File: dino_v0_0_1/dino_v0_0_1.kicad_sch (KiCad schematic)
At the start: 27 parts, among them Q1 Write Button Gate, U1 Quad AND

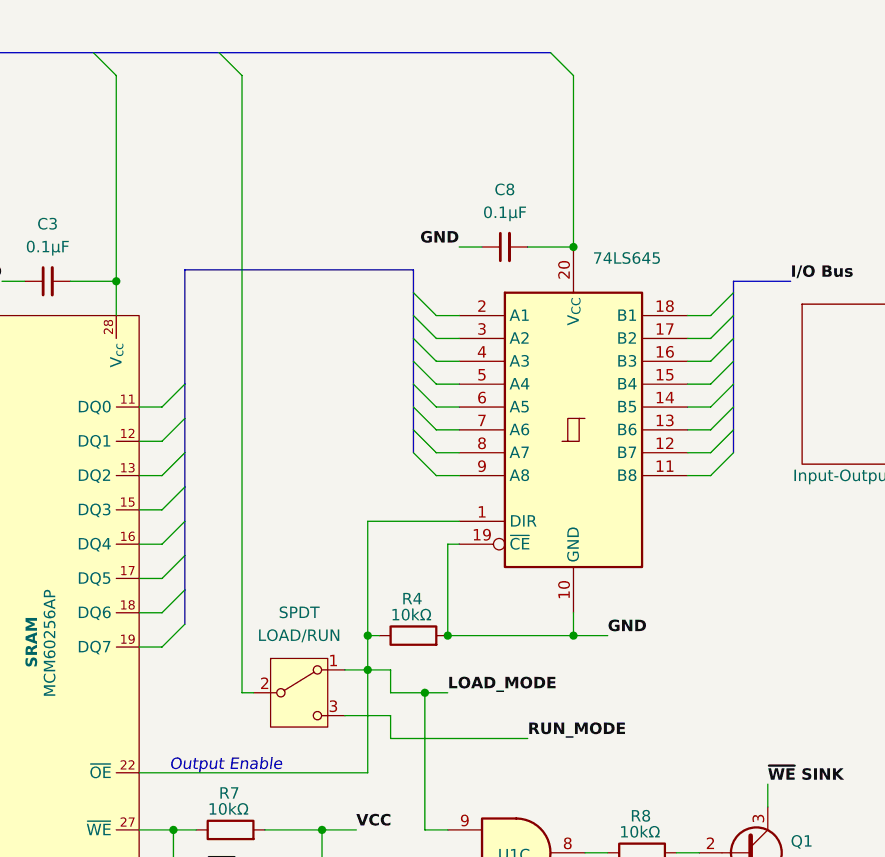
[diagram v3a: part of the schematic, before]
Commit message: Refactors circuit schematic and adds component
Repositions resistors and re-routes junctions for optimized layout.
Introduces 74LS244N component to enhance functionality.
Updates buses and wires for improved organization and signal integrity.
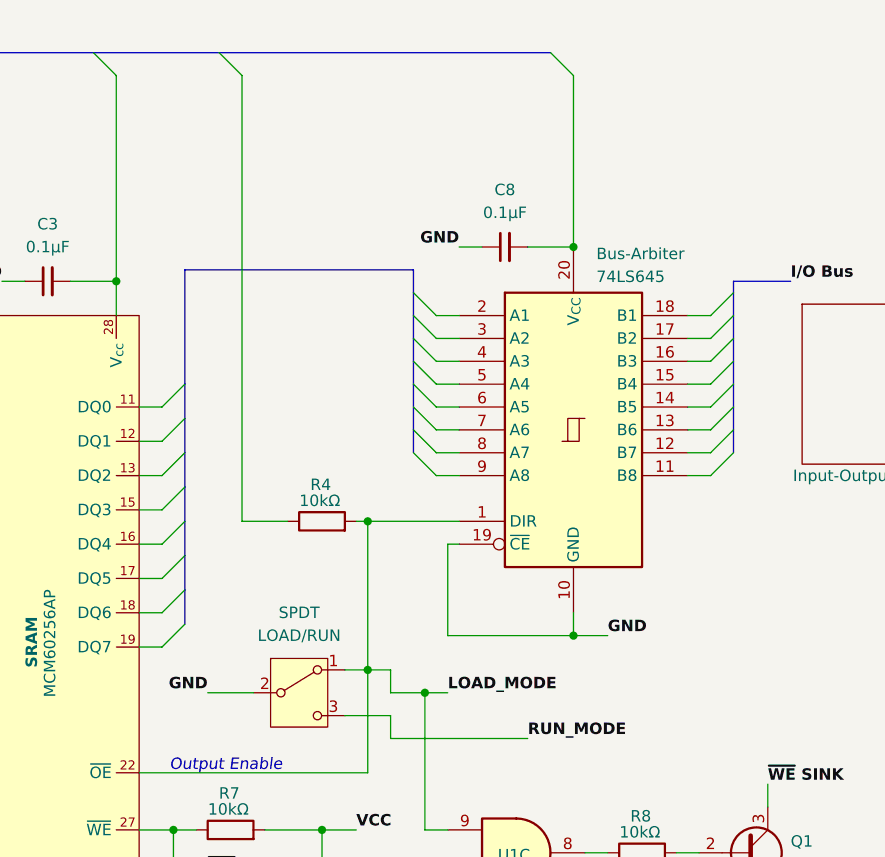
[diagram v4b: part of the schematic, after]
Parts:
- Bus-Arbiter: renamed from 74LS645; value ~ -> 74LS645
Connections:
- net GND: now also SPDT.2 (B); no longer R4.2
- net LOAD_MODE: now also R4.2; no longer R4.1
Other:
- moved on the sheet: R4
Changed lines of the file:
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@@
 	)
 	(junction
-		(at 199.39 82.55)
-		(diameter 0)
-		(color 0 0 0 0)
-	)
-	(junction
 		(at 171.45 43.18)
 		(diameter 0)
@@
 	)
 	(junction
-		(at 199.39 86.36)
+		(at 199.39 69.85)
 		(diameter 0)
 		(color 0 0 0 0)
 	)
 	(junction
-		(at 208.28 82.55)
+		(at 199.39 86.36)
 		(diameter 0)
 		(color 0 0 0 0)
@@
 	(wire
 		(pts
+			(xy 199.39 69.85) (xy 209.55 69.85)
+		)
+		(stroke
+			(width 0)
+			(type default)
+		)
+	)
+	(wire
+		(pts
 			(xy 49.53 36.83) (xy 49.53 38.1)
 		)
@@
 	(wire
 		(pts
+			(xy 199.39 69.85) (xy 199.39 86.36)
+		)
+		(stroke
+			(width 0)
+			(type default)
+		)
+	)
+	(wire
+		(pts
 			(xy 201.93 93.98) (xy 217.17 93.98)
 		)
@@
 		)
 	)
-	(wire
-		(pts
-			(xy 199.39 82.55) (xy 199.39 86.36)
-		)
-		(stroke
-			(width 0)
-			(type default)
-		)
-	)
 	(bus
 		(pts
@@
 		)
 	)
+	(wire
+		(pts
+			(xy 181.61 88.9) (xy 186.69 88.9)
+		)
+		(stroke
+			(width 0)
+			(type default)
+		)
+	)
+	(wire
+		(pts
+			(xy 198.12 69.85) (xy 199.39 69.85)
+		)
+		(stroke
+			(width 0)
+			(type default)
+		)
+	)
 	(bus
 		(pts
@@
 	(wire
 		(pts
-			(xy 185.42 20.32) (xy 185.42 88.9)
-		)
-		(stroke
-			(width 0)
-			(type default)
-		)
-	)
-	(wire
-		(pts
 			(xy 93.98 143.51) (xy 101.6 143.51)
 		)
@@
 		)
 	)
+	(wire
+		(pts
+			(xy 185.42 20.32) (xy 185.42 69.85)
+		)
+		(stroke
+			(width 0)
+			(type default)
+		)
+	)
 	(bus
 		(pts
@@
 	(wire
 		(pts
-			(xy 95.25 113.03) (xy 105.41 113.03)
+			(xy 185.42 69.85) (xy 190.5 69.85)
 		)
 		(stroke
@@
 		)
 	)
-	(bus
+	(wire
 		(pts
-			(xy 179.07 77.47) (xy 179.07 73.66)
+			(xy 95.25 113.03) (xy 105.41 113.03)
 		)
 		(stroke
@@
 		)
 	)
-	(wire
+	(bus
 		(pts
-			(xy 87.63 140.97) (xy 87.63 143.51)
+			(xy 179.07 77.47) (xy 179.07 73.66)
 		)
 		(stroke
@@
 	(wire
 		(pts
-			(xy 199.39 82.55) (xy 200.66 82.55)
+			(xy 87.63 140.97) (xy 87.63 143.51)
 		)
 		(stroke
@@
 	(wire
 		(pts
-			(xy 199.39 69.85) (xy 199.39 82.55)
-		)
-		(stroke
-			(width 0)
-			(type default)
-		)
-	)
-	(wire
-		(pts
 			(xy 234.95 59.69) (xy 237.49 59.69)
 		)
@@
 	(wire
 		(pts
-			(xy 186.69 88.9) (xy 185.42 88.9)
-		)
-		(stroke
-			(width 0)
-			(type default)
-		)
-	)
-	(wire
-		(pts
 			(xy 234.95 62.23) (xy 237.49 62.23)
 		)
@@
 		)
 	)
-	(wire
-		(pts
-			(xy 209.55 69.85) (xy 199.39 69.85)
-		)
-		(stroke
-			(width 0)
-			(type default)
-		)
-	)
 	(bus
 		(pts
@@
 		)
 	)
+	(label "GND"
+		(at 181.61 88.9 180)
+		(effects
+			(font
+				(size 1.27 1.27)
+				(thickness 0.254)
+				(bold yes)
+				(color 0 0 0 1)
+			)
+			(justify right bottom)
+		)
+	)
 	(label "RUN_MODE"
 		(at 60.96 59.69 180)
@@
 		(on_board yes)
 		(dnp no)
-		(fields_autoplaced yes)
-		(property "Reference" "74LS645"
-			(at 224.3933 40.64 0)
+		(property "Reference" "Bus-Arbiter"
+			(at 224.79 40.132 0)
 			(effects
 				(font
@@
 			)
 		)
-		(property "Value" "~"
-			(at 224.3933 43.18 0)
+		(property "Value" "74LS645"
+			(at 224.79 42.672 0)
 			(effects
 				(font
@@
 			(project ""
 				(path "/e43166a5-d972-471d-b3cf-9f4f12c7f541"
-					(reference "74LS645")
+					(reference "Bus-Arbiter")
 					(unit 1)
 				)
@@
 	(symbol
 		(lib_id "Device:R")
-		(at 204.47 82.55 90)
+		(at 194.31 69.85 90)
 		(unit 1)
 		(exclude_from_sim no)
@@
 		(dnp no)
 		(property "Reference" "R4"
-			(at 205.486 78.486 90)
+			(at 195.326 65.786 90)
 			(effects
 				(font
@@
 		)
 		(property "Value" "10kΩ"
-			(at 206.502 80.264 90)
+			(at 196.342 67.564 90)
 			(effects
 				(font
@@
 		)
 		(property "Footprint" ""
-			(at 204.47 84.328 90)
+			(at 194.31 71.628 90)
 			(effects
 				(font
@@
 		)
 		(property "Datasheet" "~"
-			(at 204.47 82.55 0)
+			(at 194.31 69.85 0)
 			(effects
 				(font
@@
 		)
 		(property "Description" "Resistor"
-			(at 204.47 82.55 0)
+			(at 194.31 69.85 0)
 			(effects
 				(font
